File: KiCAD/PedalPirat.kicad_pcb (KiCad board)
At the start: 2 copper layers, 37 parts, among them IC1 IS32IO1028A-GRLA2-TR, IC2 IS31CS8979-QFLS2-TR

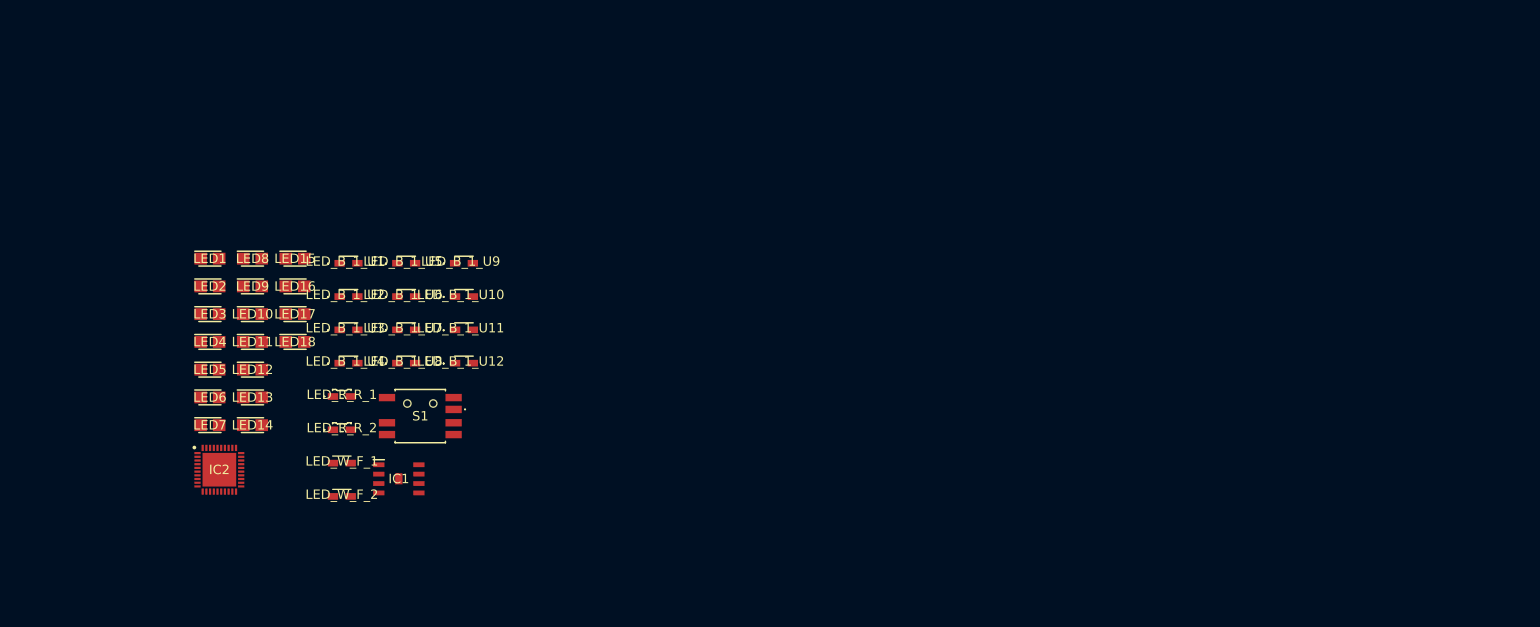
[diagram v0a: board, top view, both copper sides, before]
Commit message: updated structure, new components
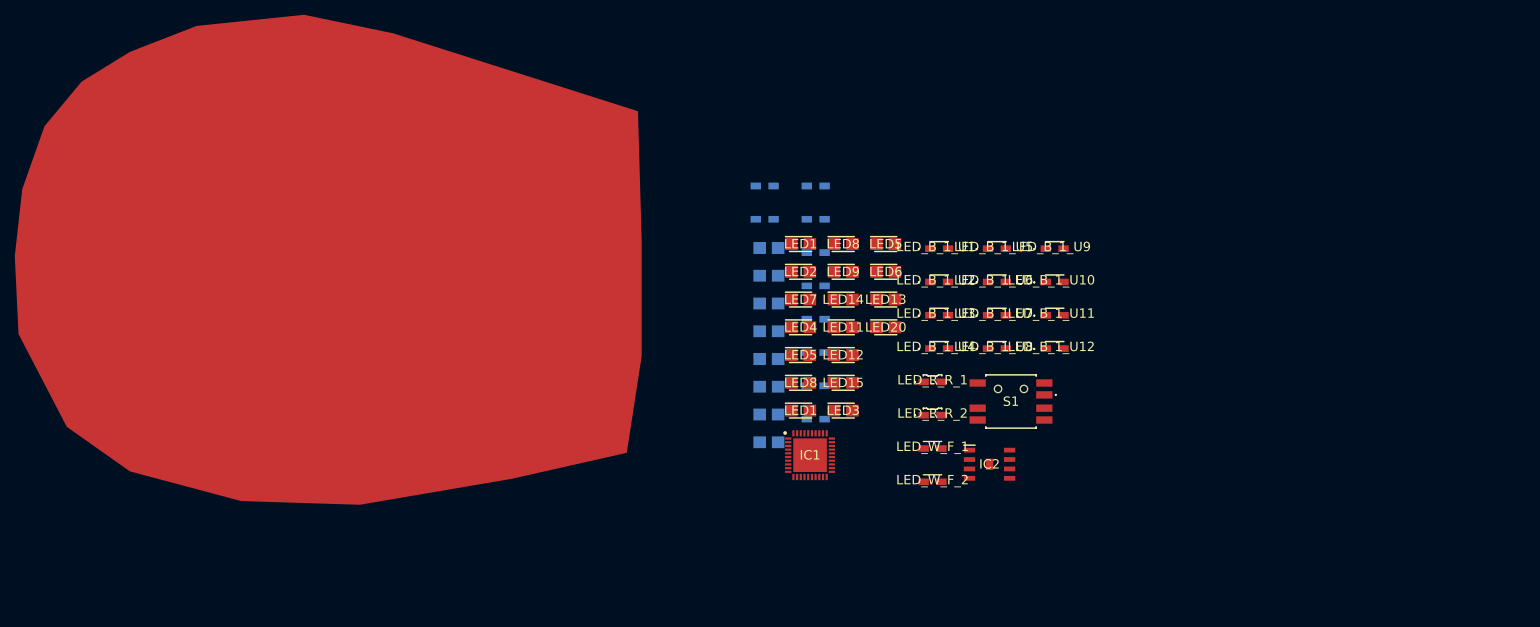
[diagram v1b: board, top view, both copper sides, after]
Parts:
- added LED10: AA3021SYSK_J3-TR, SamacSys_Parts:LEDM3020X150N, B.Cu at (162.8, 73.7)
- added LED11: AA3021SYSK_J3-TR, SamacSys_Parts:LEDM3020X150N, B.Cu at (162.8, 77.4)
- added LED12: AA3021SYSK_J3-TR, SamacSys_Parts:LEDM3020X150N, B.Cu at (162.8, 81.2)
- added LED16: AA3021SYSK_J3-TR, SamacSys_Parts:LEDM3020X150N, B.Cu at (162.8, 84.9)
- added LED17: AA3021SYSK_J3-TR, SamacSys_Parts:LEDM3020X150N, B.Cu at (162.8, 88.7)
- added LED18: AA3021SYSK_J3-TR, SamacSys_Parts:LEDM3020X150N, B.Cu at (162.8, 92.4)
- added LED19: AA3021SYSK_J3-TR, SamacSys_Parts:LEDM3020X150N, B.Cu at (162.8, 96.2)
- added LED2: AA2810ASES_J3, SamacSys_Parts:AA2810ASESJ3, B.Cu at (162.2, 61.3)
- added LED4: AA2810ASES_J3, SamacSys_Parts:AA2810ASESJ3, B.Cu at (162.2, 65.8)
- added LED9: AA3021SYSK_J3-TR, SamacSys_Parts:LEDM3020X150N, B.Cu at (162.8, 69.9)
- added LED_B_1_U10: AA2810AQBS_D, SamacSys_Parts:AA2810AQBSD, B.Cu at (169.1, 84.0)
- added LED_B_1_U11: AA2810AQBS_D, SamacSys_Parts:AA2810AQBSD, B.Cu at (169.1, 88.5)
- added LED_B_1_U12: AA2810AQBS_D, SamacSys_Parts:AA2810AQBSD, B.Cu at (169.1, 93.0)
- added LED_B_1_U3: AA2810AQBS_D, SamacSys_Parts:AA2810AQBSD, B.Cu at (169.1, 61.5)
- added LED_B_1_U4: AA2810AQBS_D, SamacSys_Parts:AA2810AQBSD, B.Cu at (169.1, 66.0)
- added LED_B_1_U5: AA2810AQBS_D, SamacSys_Parts:AA2810AQBSD, B.Cu at (169.1, 70.5)
- added LED_B_1_U6: AA2810AQBS_D, SamacSys_Parts:AA2810AQBSD, B.Cu at (169.1, 75.0)
- added LED_B_1_U9: AA2810AQBS_D, SamacSys_Parts:AA2810AQBSD, B.Cu at (169.1, 79.5)
- moved LED_B_1_U1 79.8 mm to (185.8, 70.0)
- moved LED_B_1_U10 79.8 mm to (201.4, 74.5)
- moved LED_B_1_U11 79.8 mm to (201.4, 79.0)
- moved LED_B_1_U12 79.8 mm to (201.4, 83.5)
- moved LED_B_1_U2 79.8 mm to (185.8, 74.5)
- moved LED_B_1_U3 79.8 mm to (185.8, 79.0)
- moved LED_B_1_U4 79.8 mm to (185.8, 83.5)
- moved LED_B_1_U9 79.8 mm to (201.4, 70.0)
- moved LED_R_R_1 79.8 mm to (184.9, 87.8)
- moved LED_R_R_2 79.8 mm to (184.9, 92.2)
- moved LED_W_F_1 79.8 mm to (184.9, 96.7)
- moved LED_W_F_2 79.8 mm to (184.9, 101.2)
- moved IC1 79.8 mm to (168.3, 97.9)
- moved IC2 79.8 mm to (192.6, 99.1)
- moved LED_B_1_U5 79.8 mm to (193.6, 70.0)
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- renumbered IC2 to IC1, IC1 to IC2, LED7 to LED1, LED17 to LED13, LED10 to LED14, LED13 to LED15, LED18 to LED20, LED14 to LED3, LED15 to LED5, LED16 to LED6, LED3 to LED7, LED6 to LED8
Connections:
- net Net-(IC1-RSTN) renamed RSTN
- IC1 pad 1: unconnected-(IC2-OUT14-Pad1) -> B6-Side
- IC1 pad 10: unconnected-(IC2-P04-Pad10) -> S-Brake
- IC1 pad 11: unconnected-(IC2-P03-Pad11) -> S-Ext-2
- IC1 pad 12: unconnected-(IC2-P02-Pad12) -> S-Ext-1
- IC1 pad 13: unconnected-(IC2-P01-Pad13) -> S-Grip-Bot
- IC1 pad 14: unconnected-(IC2-P00-Pad14) -> S-Grip-RGB
- IC1 pad 17: unconnected-(IC2-VDD_2-Pad17) -> +5V
- IC1 pad 2: unconnected-(IC2-OUT15-Pad2) -> B6-Top
- IC1 pad 20: unconnected-(IC2-P17-Pad20) -> ENLIN
- IC1 pad 21: unconnected-(IC2-P16-Pad21) -> RXD
- IC1 pad 22: unconnected-(IC2-P15-Pad22) -> TXD
- IC1 pad 23: unconnected-(IC2-P12/P13/P14-Pad23) -> S-Bar-2
- IC1 pad 24: unconnected-(IC2-INTB-Pad24) -> S-Bar-1
- IC1 pad 25: unconnected-(IC2-VSSO_2-Pad25) -> GND
- IC1 pad 26: Net-(IC2-OUT1) -> W-Side
- IC1 pad 27: Net-(IC2-OUT2) -> W-Top
- IC1 pad 28: Net-(IC2-OUT3) -> R-Side
- IC1 pad 29: unconnected-(IC2-OUT4-Pad29) -> B1-Side
- IC1 pad 3: unconnected-(IC2-OUT16-Pad3) -> S-Grip-R
- IC1 pad 30: unconnected-(IC2-OUT5-Pad30) -> B1-Top
- IC1 pad 31: unconnected-(IC2-OUT6-Pad31) -> B2-Side
- IC1 pad 32: unconnected-(IC2-OUT7-Pad32) -> B2-Top
- IC1 pad 33: unconnected-(IC2-OUT8-Pad33) -> B3-Side
- IC1 pad 34: unconnected-(IC2-OUT9-Pad34) -> B3-Top
- IC1 pad 35: unconnected-(IC2-VSSO_3-Pad35) -> GND
- IC1 pad 36: unconnected-(IC2-VSSO_4-Pad36) -> GND
- IC1 pad 37: unconnected-(IC2-OUT10-Pad37) -> B4-Side
- IC1 pad 38: unconnected-(IC2-OUT11-Pad38) -> B4-Top
- IC1 pad 39: unconnected-(IC2-OUT12-Pad39) -> B5-Side
- IC1 pad 4: unconnected-(IC2-OUT17-Pad4) -> S-Grip-G
- IC1 pad 40: unconnected-(IC2-OUT13-Pad40) -> B5-Top
- IC1 pad 41: unconnected-(IC2-EP-Pad41) -> GND
- IC1 pad 5: unconnected-(IC2-OUT18-Pad5) -> S-Grip-B
- IC1 pad 6: unconnected-(IC2-VSSO_1-Pad6) -> GND
- IC1 pad 7: unconnected-(IC2-REXT-Pad7) -> Net-(IC1-REXT)
- IC1 pad 8: unconnected-(IC2-SDB-Pad8) -> SDB
- IC1 pad 9: unconnected-(IC2-VDD_1-Pad9) -> +5V
- IC2 pad 1: unconnected-(IC1-VBAT-Pad1) -> +5V
- IC2 pad 2: unconnected-(IC1-EN-Pad2) -> ENLIN
- IC2 pad 3: unconnected-(IC1-GND-Pad3) -> GND
- IC2 pad 4: unconnected-(IC1-LIN-Pad4) -> Net-(IC2-LIN)
- IC2 pad 5: unconnected-(IC1-RXD-Pad5) -> RXD
- IC2 pad 6: unconnected-(IC1-TXD-Pad6) -> TXD
- IC2 pad 8: unconnected-(IC1-VCC-Pad8) -> VCC-IO
- IC2 pad 9: unconnected-(IC1-EPAD-Pad9) -> GND
- LED1 pad 1: Net-(IC2-OUT2) -> Net-(LED1-K)
- LED1 pad 2: Net-(LED14-K) (its old number) -> Net-(LED1-A)
- LED14 pad 2: unconnected-(LED10-A-Pad2) -> +5V
- LED15 pad 2: unconnected-(LED13-A-Pad2) -> +5V
- LED20 pad 2: VCC -> +5V
- LED3 pad 1: Net-(LED14-K) (its old number) -> Net-(LED1-A)
- LED7 pad 1: unconnected-(LED3-K-Pad1) -> Net-(LED7-K)
- LED8 pad 1: unconnected-(LED6-K-Pad1) -> Net-(LED8-K)
- LED_B_1_U1 pad 1: unconnected-(LED_B_1_U1-K-Pad1) -> Net-(LED_B_1_U1-K)
- LED_B_1_U2 pad 1: unconnected-(LED_B_1_U2-K-Pad1) -> Net-(LED_B_1_U2-K)
- LED_B_1_U7 pad 2: unconnected-(LED_B_1_U7-A-Pad2) -> +5V
- LED_B_1_U8 pad 2: unconnected-(LED_B_1_U8-A-Pad2) -> +5V
- LED_W_F_1 pad 1: Net-(IC2-OUT1) -> Net-(LED_W_F_1-K)
- LED_W_F_2 pad 2: VCC -> +5V

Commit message: dasasd
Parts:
- added IC1: IS31CS8979-QFLS2-TR, SamacSys_Parts:QFN50P600X600X80-41N-D, F.Cu at (221.8, 97.4)
- added IC2: IS32IO1028A-GRLA2-TR, SamacSys_Parts:SOIC127P600X170-9N, F.Cu at (250.0, 103.5)
- added IC3: IS31CS8979-QFLS2-TR, SamacSys_Parts:QFN50P600X600X80-41N-D, F.Cu at (232.2, 115.8)
- added IC4: IS32IO1028A-GRLA2-TR, SamacSys_Parts:SOIC127P600X170-9N, F.Cu at (232.3, 108.3)
- added IC5: IS31CS8979-QFLS2-TR, SamacSys_Parts:QFN50P600X600X80-41N-D, F.Cu at (221.8, 115.8)
- added IC6: IS32IO1028A-GRLA2-TR, SamacSys_Parts:SOIC127P600X170-9N, F.Cu at (221.8, 108.3)
- added IC7: IS32LT3183A-GRLA3-TR, SamacSys_Parts:SOIC127P600X170-9N, F.Cu at (261.5, 109.0)
- added LED1: AA3021SESK_J3-TR, SamacSys_Parts:LEDM3020X150N, F.Cu at (220.5, 68.9)
- added LED10: AA3021SYSK_J3-TR, SamacSys_Parts:LEDM3020X150N, F.Cu at (226.2, 68.9)
- added LED11: AA3021SYSK_J3-TR, SamacSys_Parts:LEDM3020X150N, F.Cu at (226.2, 72.6)
- added LED12: AA3021SYSK_J3-TR, SamacSys_Parts:LEDM3020X150N, F.Cu at (226.2, 76.4)
- added LED13: AA3021SESK_J3-TR, SamacSys_Parts:LEDM3020X150N, F.Cu at (226.2, 80.1)
- added LED14: AA3021SYSK_J3-TR, SamacSys_Parts:LEDM3020X150N, F.Cu at (226.2, 83.9)
- added LED15: AA3021SYSK_J3-TR, SamacSys_Parts:LEDM3020X150N, F.Cu at (226.2, 87.6)
- added LED16: AA3021SYSK_J3-TR, SamacSys_Parts:LEDM3020X150N, F.Cu at (226.2, 91.4)
- added LED17: AA3021SYSK_J3-TR, SamacSys_Parts:LEDM3020X150N, F.Cu at (232.0, 68.9)
- added LED18: AA3021SYSK_J3-TR, SamacSys_Parts:LEDM3020X150N, F.Cu at (232.0, 72.6)
- added LED19: AA3021SYSK_J3-TR, SamacSys_Parts:LEDM3020X150N, F.Cu at (232.0, 76.4)
- added LED2: AA2810ASES_J3, SamacSys_Parts:AA2810ASESJ3, F.Cu at (238.3, 87.2)
- added LED20: AA3021SESK_J3-TR, SamacSys_Parts:LEDM3020X150N, F.Cu at (232.0, 80.1)
- added LED21: AA3021SYSK_J3-TR, SamacSys_Parts:LEDM3020X150N, F.Cu at (239.3, 113.5)
- added LED22: AA3021SYSK_J3-TR, SamacSys_Parts:LEDM3020X150N, F.Cu at (247.0, 113.5)
- added LED3: AA3021SESK_J3-TR, SamacSys_Parts:LEDM3020X150N, F.Cu at (220.5, 72.6)
- added LED4: AA2810ASES_J3, SamacSys_Parts:AA2810ASESJ3, F.Cu at (238.3, 91.8)
- added LED5: AA3021SESK_J3-TR, SamacSys_Parts:LEDM3020X150N, F.Cu at (220.5, 76.4)
- added LED6: AA3021SESK_J3-TR, SamacSys_Parts:LEDM3020X150N, F.Cu at (220.5, 80.1)
- added LED7: AA3021SYSK_J3-TR, SamacSys_Parts:LEDM3020X150N, F.Cu at (220.5, 83.9)
- added LED8: AA3021SYSK_J3-TR, SamacSys_Parts:LEDM3020X150N, F.Cu at (220.5, 87.6)
- added LED9: AA3021SYSK_J3-TR, SamacSys_Parts:LEDM3020X150N, F.Cu at (220.5, 91.4)
- added LED_B_1_U1: AA2810AQBS_D, SamacSys_Parts:AA2810AQBSD, F.Cu at (239.2, 69.5)
- added LED_B_1_U10: AA2810AQBS_D, SamacSys_Parts:AA2810AQBSD, F.Cu at (254.8, 74.0)
- added LED_B_1_U11: AA2810AQBS_D, SamacSys_Parts:AA2810AQBSD, F.Cu at (254.8, 78.5)
- added LED_B_1_U12: AA2810AQBS_D, SamacSys_Parts:AA2810AQBSD, F.Cu at (254.8, 83.0)
- added LED_B_1_U2: AA2810AQBS_D, SamacSys_Parts:AA2810AQBSD, F.Cu at (239.2, 74.0)
- added LED_B_1_U3: AA2810AQBS_D, SamacSys_Parts:AA2810AQBSD, F.Cu at (239.2, 78.5)
- added LED_B_1_U4: AA2810AQBS_D, SamacSys_Parts:AA2810AQBSD, F.Cu at (239.2, 83.0)
- added LED_B_1_U5: AA2810AQBS_D, SamacSys_Parts:AA2810AQBSD, F.Cu at (247.0, 69.5)
- added LED_B_1_U6: AA2810AQBS_D, SamacSys_Parts:AA2810AQBSD, F.Cu at (247.0, 74.0)
- added LED_B_1_U7: AA2810AQBS_D, SamacSys_Parts:AA2810AQBSD, F.Cu at (247.0, 78.5)
- added LED_B_1_U8: AA2810AQBS_D, SamacSys_Parts:AA2810AQBSD, F.Cu at (247.0, 83.0)
- added LED_B_1_U9: AA2810AQBS_D, SamacSys_Parts:AA2810AQBSD, F.Cu at (254.8, 69.5)
- added LED_W_F_1: AA2810AVW1S, SamacSys_Parts:AA2810AVW1S, F.Cu at (238.3, 96.2)
- added LED_W_F_2: AA2810AVW1S, SamacSys_Parts:AA2810AVW1S, F.Cu at (238.3, 100.7)
- added S1: 228EMVARGBFR, SamacSys_Parts:228EMVARGBFR, F.Cu at (248.9, 90.2)
